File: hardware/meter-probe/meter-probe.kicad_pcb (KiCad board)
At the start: 4 copper layers, 40 x 68 mm, 57 parts, among them J1 Cable, SW1 Sensor Button, U1 TSL2585, U2 USBLC6-2SC6, U3 MIC5365-1.8YC5, U4 FT260Q, U5 CAT24C08

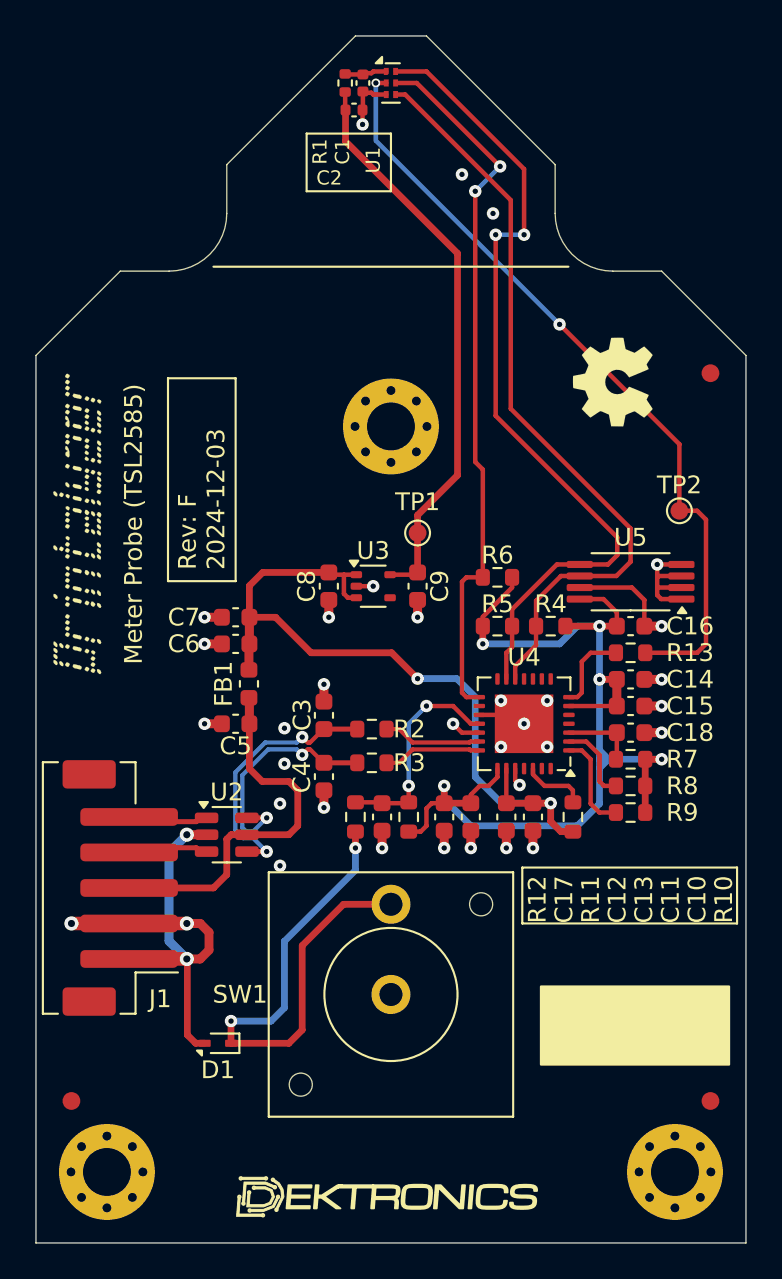
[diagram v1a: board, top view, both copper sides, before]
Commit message: Change light sensor on peripherals
Ref #85
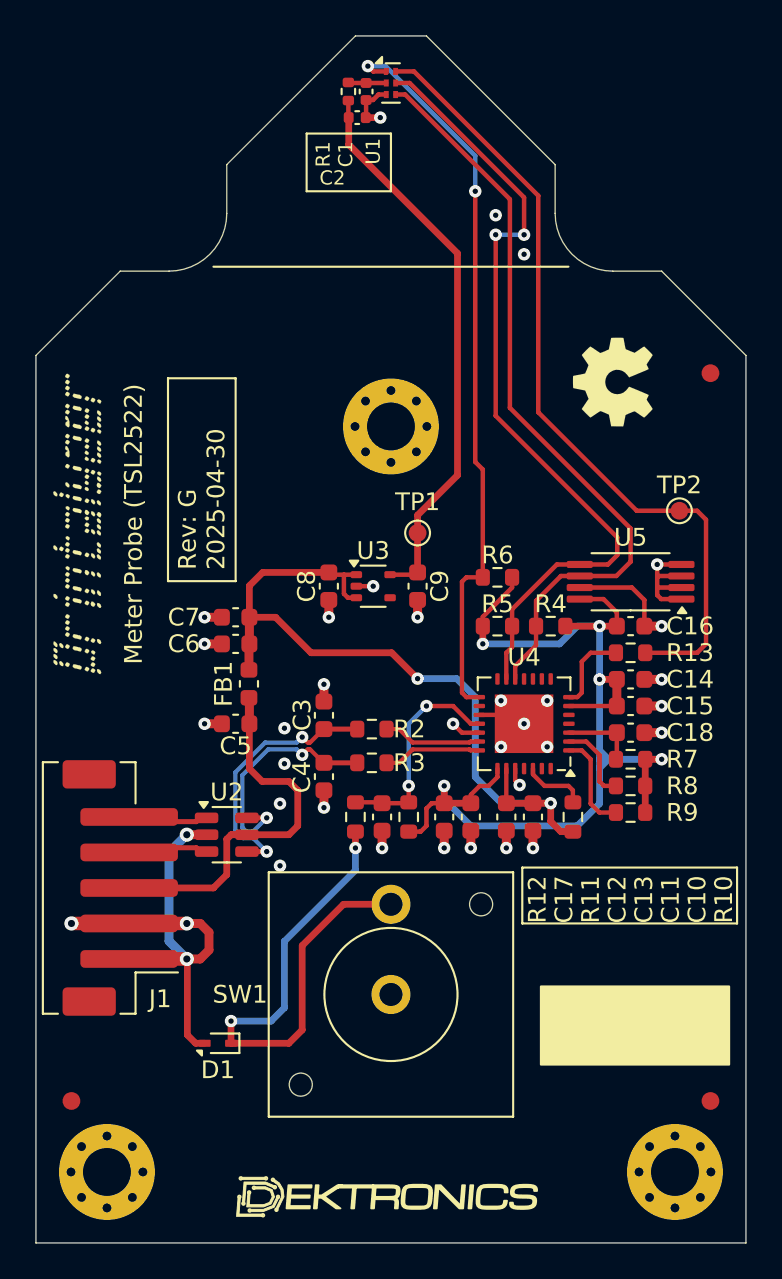
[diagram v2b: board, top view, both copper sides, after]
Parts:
- U1: value TSL2585 -> TSL2522
- moved C1 0.51 mm to (118.6, 63.1)
- moved R1 0.51 mm to (117.6, 63.1)
- moved C2 0.46 mm to (118.1, 64.6)
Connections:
- U1 pad 1: Net-(U1-VDD) -> /TSL_INT
- U1 pad 2: /TSL_VSYNC -> Net-(U1-VDD)
- U1 pad 5: /TSL_INT -> /I2C_SDA
- U1 pad 6: /I2C_SDA -> /TSL_VSYNC
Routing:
- net /TSL_VSYNC: track 44.1 -> 45.7 mm, vias 2 -> 0
- net /TSL_INT: track 40.3 -> 41.8 mm
- net /I2C_SDA: track 47.0 -> 45.7 mm
- net +1V8: track 32.0 -> 31.5 mm
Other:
- board text added: "Meter Probe (TSL2522)"
- board text removed: "Meter Probe (TSL2585)"

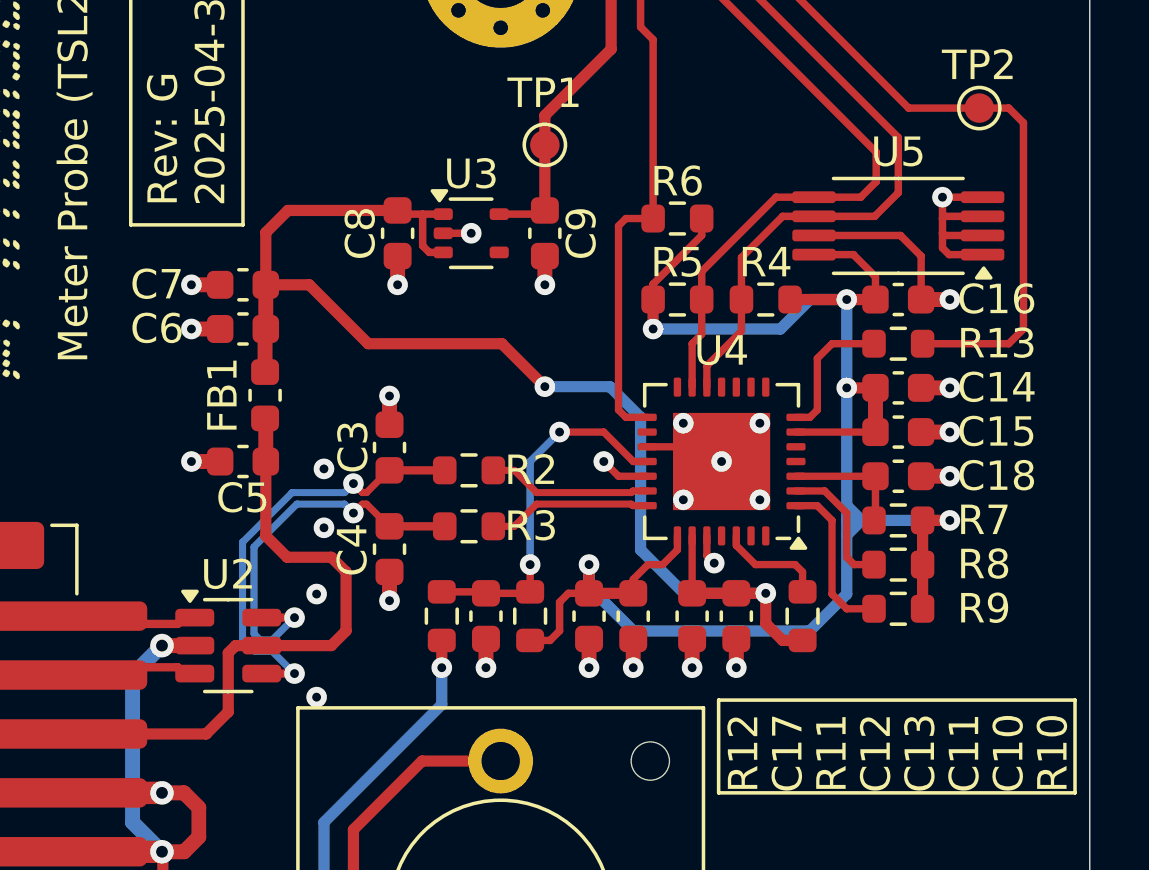
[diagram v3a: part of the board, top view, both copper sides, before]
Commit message: Update peripheral projects for KiCad v10
The v10 update fortunately resulted in no schematic changes needed.

However, there were several footprint/model updates for the PCBs.  Any
updates with visible copper layer changes were held back (aside from 3D
model fixes), while updates only affecting cosmetic silkscreen areas
were pulled in.
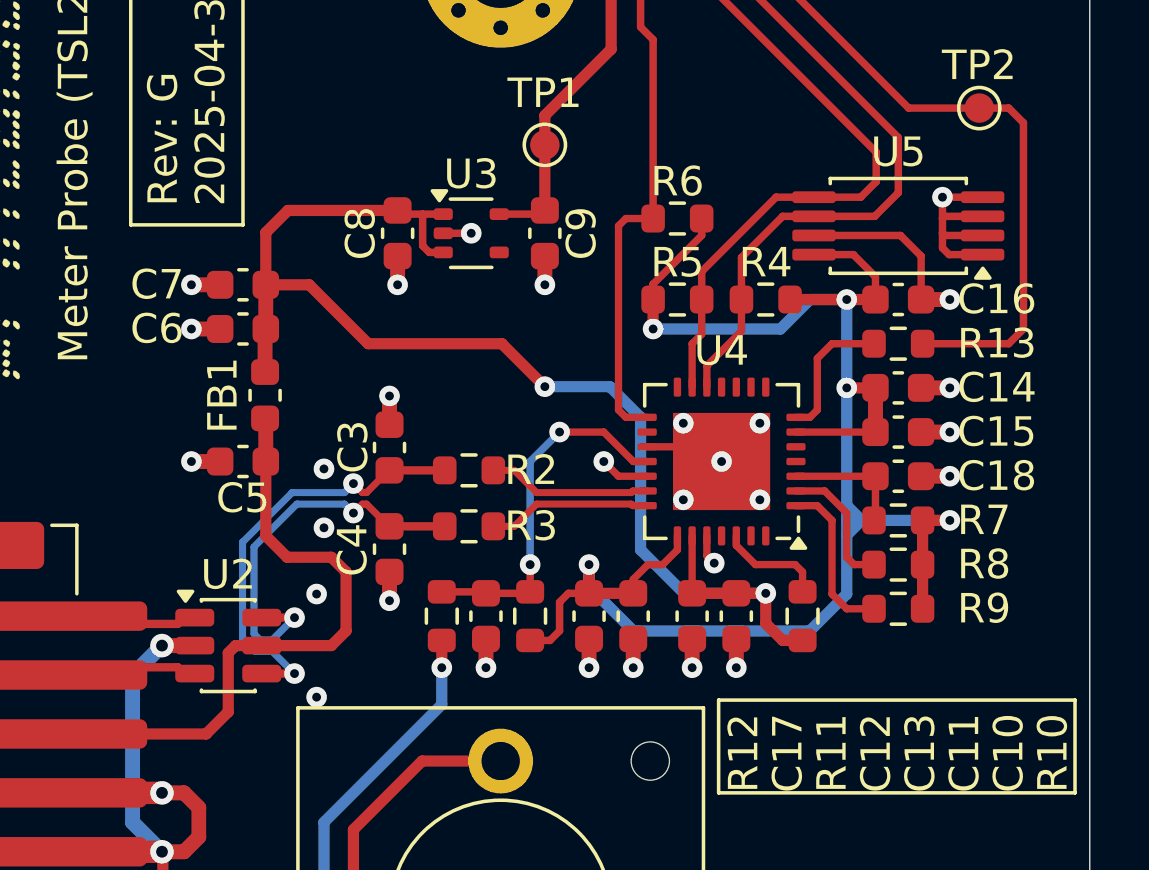
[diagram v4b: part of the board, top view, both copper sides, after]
